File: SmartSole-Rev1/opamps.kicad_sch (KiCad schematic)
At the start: 19 parts, among them U1 MCP6004, U2 MCP6004, U3 AD1583

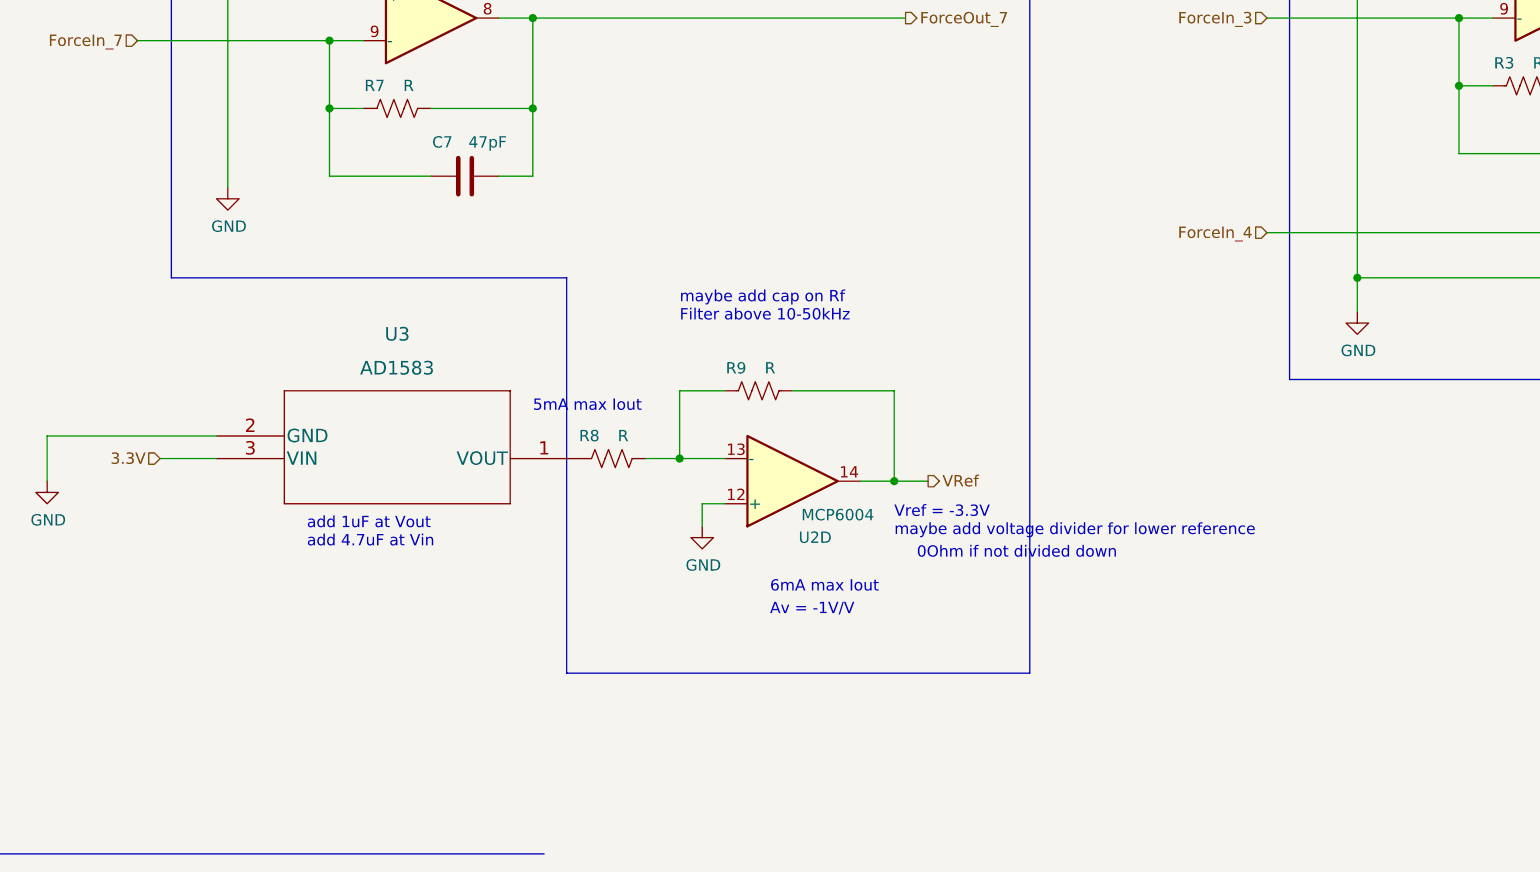
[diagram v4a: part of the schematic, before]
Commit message: Completed updates for schematic and PCB as noted from last review with rachel, DRC only warnings
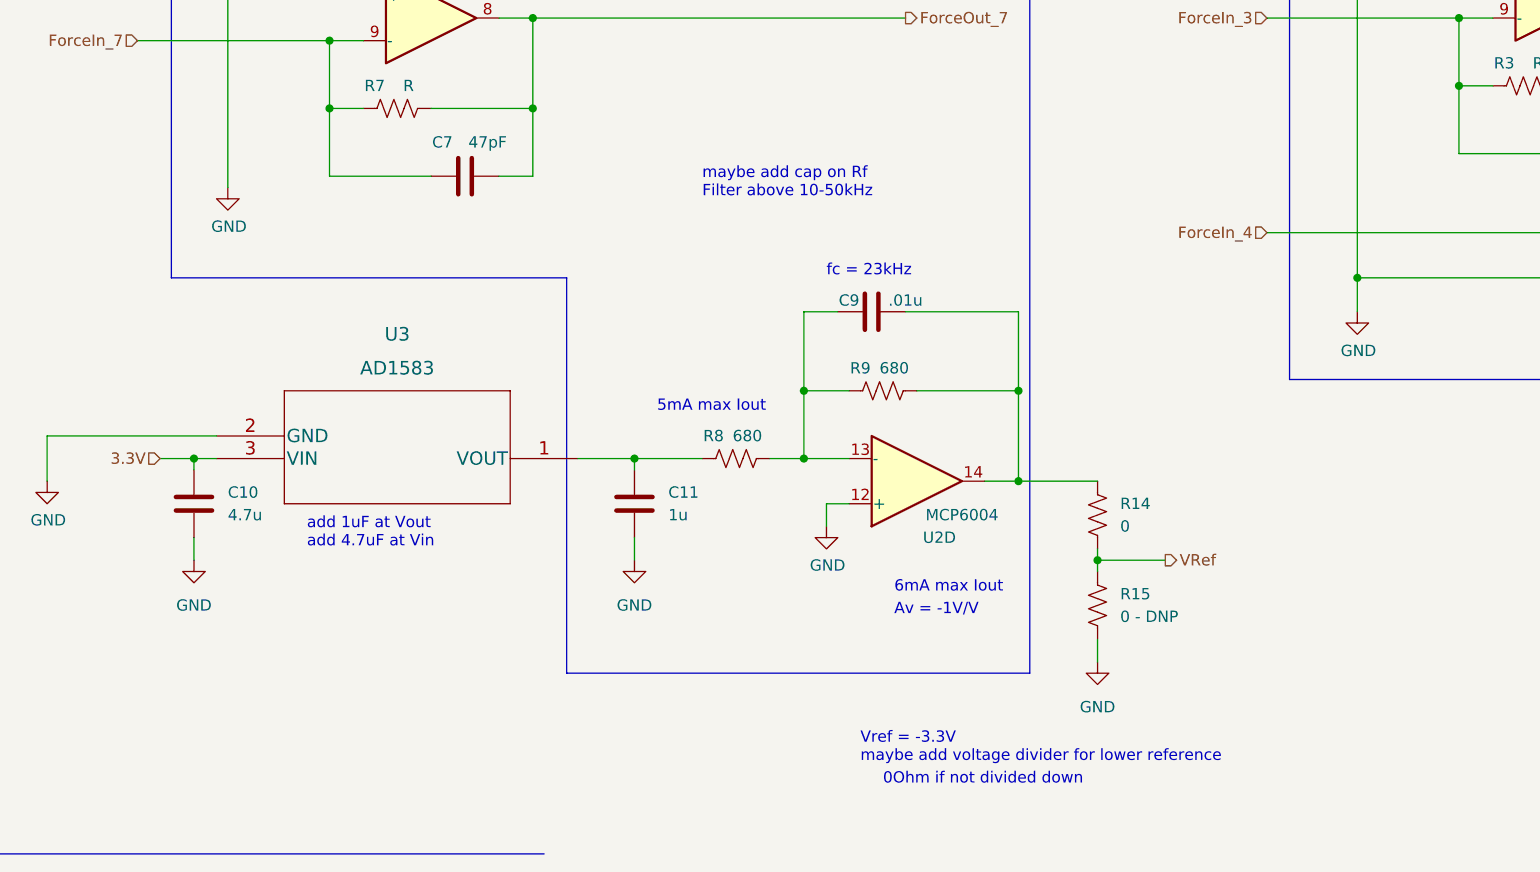
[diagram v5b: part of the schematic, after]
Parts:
- added C10: 4.7u, Capacitor_SMD:C_0603_1608Metric, symbol Device:C
- added C11: 1u, Capacitor_SMD:C_0603_1608Metric, symbol Device:C
- added C9: .01u, Capacitor_SMD:C_0603_1608Metric, symbol Device:C
- added R14: 0, Resistor_SMD:R_0603_1608Metric, symbol Device:R_US
- added R15: 0 - DNP, Resistor_SMD:R_0603_1608Metric, symbol Device:R_US
- R8, R9: value R -> 680
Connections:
- net 3.3V: now also C10.1
- net GND: now also C10.2, C11.2, R15.2
- net VRef: now also R14.1, R15.1; no longer R9.2, U2.14
- net at R8.2, R9.1, U2.13 (-): now also C9.1
- net at R8.1, U3.1 (VOUT): now also C11.1
- new net: C9.2, R14.2, R9.2, U2.14
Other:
- note added: "fc = 23kHz"
- moved on the sheet: R8, R9, U2D

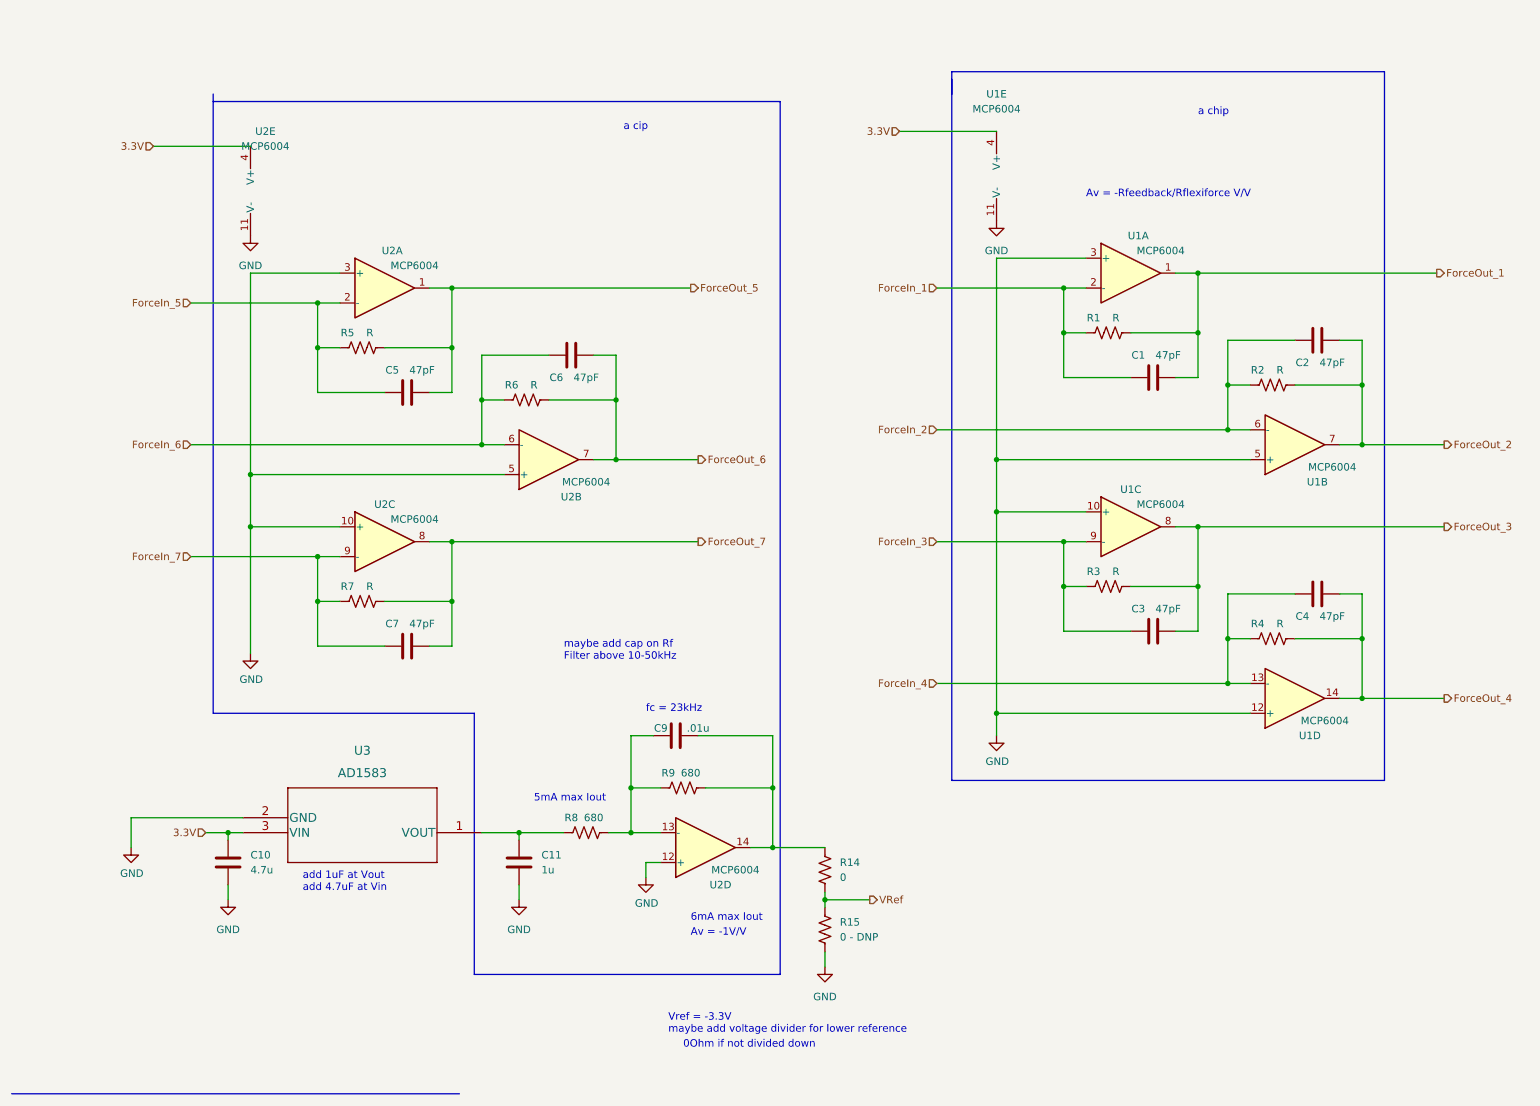
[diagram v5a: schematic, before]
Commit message: changed to non-inverting config
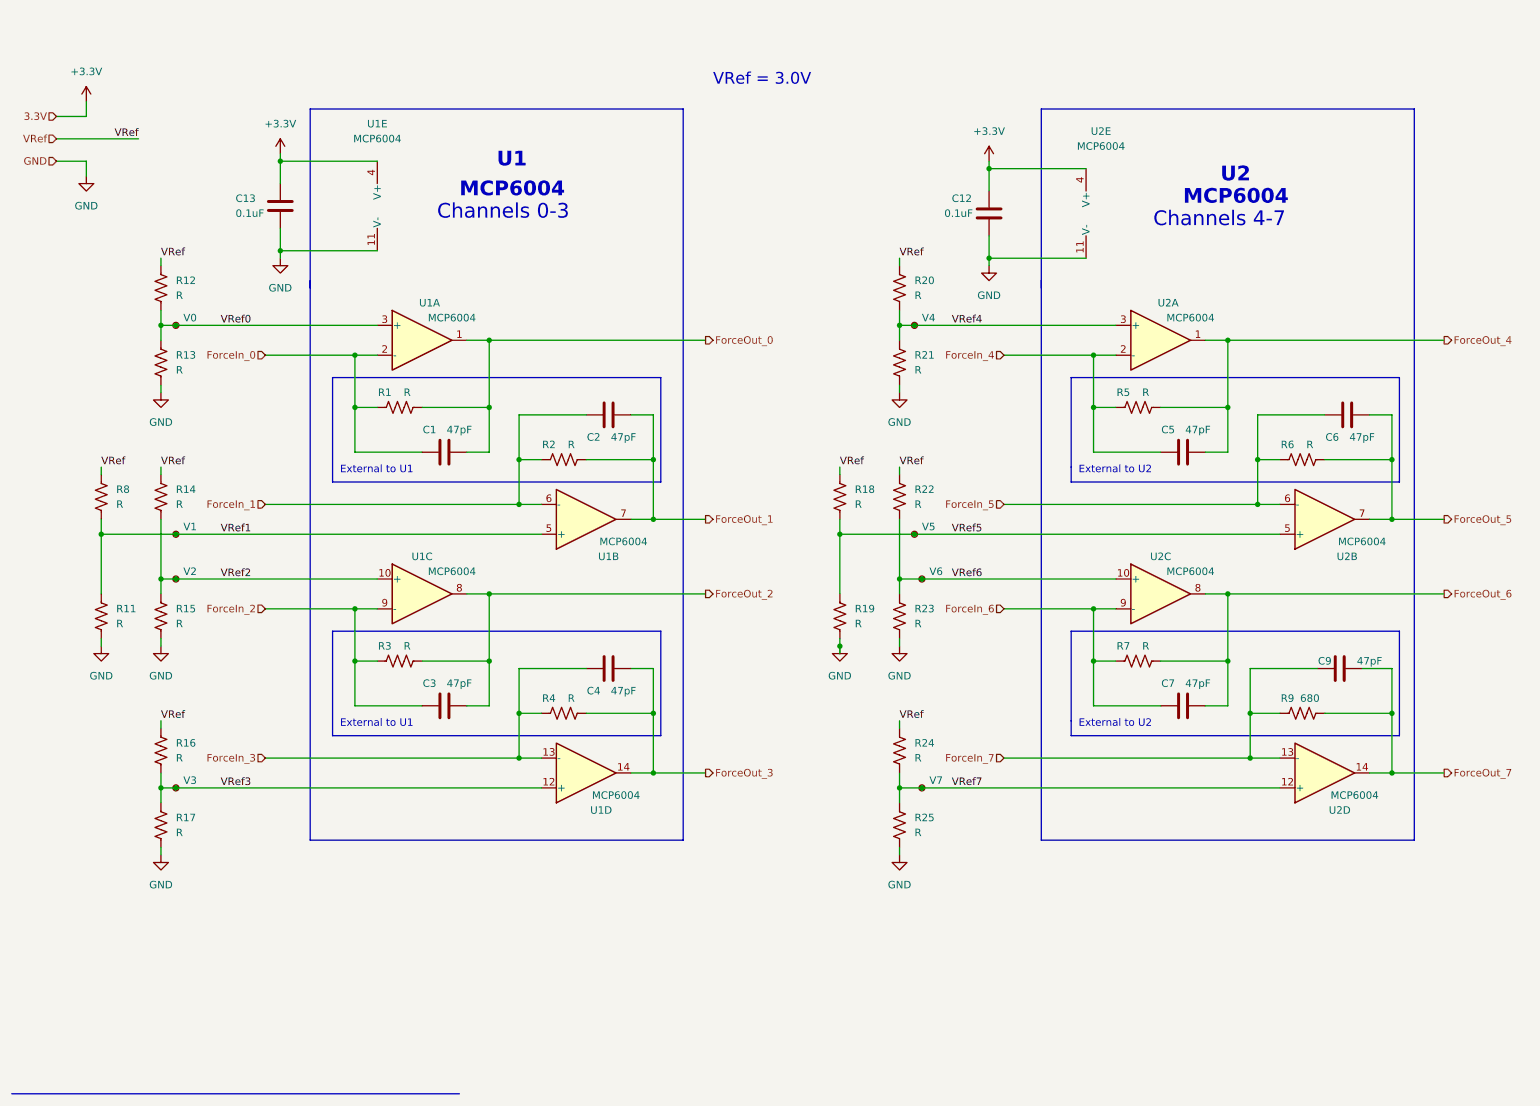
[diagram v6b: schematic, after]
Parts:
- removed C10: 4.7u, Capacitor_SMD:C_0603_1608Metric, symbol Device:C
- removed C11: 1u, Capacitor_SMD:C_0603_1608Metric, symbol Device:C
- removed U3: AD1583, CapstoneLibrary:AD1583ARTZ-Reel7, symbol CapstoneLibrary:AD1583
- added C12, C13: 0.1uF, Capacitor_SMD:C_0603_1608Metric, symbol Device:C
- added R11, R12, R13, R16, R17, R18, R19, R20, R21, R22, R23, R24, R25: R, Resistor_SMD:R_0603_1608Metric, symbol Device:R_US
- added V0, V1, V2, V3, V4, V5, V6, V7: TestPoint_Small, TestPoint:TestPoint_THTPad_1.5x1.5mm_Drill0.7mm, symbol Connector:TestPoint_Small
- C9: value .01u -> 47pF
- R14: value 0 -> R
- R15: value 0 - DNP -> R
- R8: value 680 -> R
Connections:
- net ForceIn_1: now also C2.2, R2.1, U1.6 (-); no longer C1.2, R1.1, U1.2 (-)
- net ForceIn_2: now also C3.2, R3.1, U1.9 (-); no longer C2.2, R2.1, U1.6 (-)
- net ForceIn_3: now also C4.2, R4.1, U1.13 (-); no longer C3.2, R3.1, U1.9 (-)
- net ForceIn_4: now also C5.2, R5.1, U2.2 (-); no longer C4.2, R4.1, U1.13 (-)
- net ForceIn_5: now also C6.2, R6.1, U2.6 (-); no longer C5.2, R5.1, U2.2 (-)
- net ForceIn_6: now also C7.2, R7.1, U2.9 (-); no longer C6.2, R6.1, U2.6 (-)
- net ForceIn_7: now also C9.1, R9.1, U2.13 (-); no longer C7.2, R7.1, U2.9 (-)
- net ForceOut_1: now also C2.1, R2.2, U1.7; no longer C1.1, R1.2, U1.1
- net ForceOut_2: now also C3.1, R3.2, U1.8; no longer C2.1, R2.2, U1.7
- net ForceOut_3: now also C4.1, R4.2, U1.14; no longer C3.1, R3.2, U1.8
- net ForceOut_4: now also C5.1, R5.2, U2.1; no longer C4.1, R4.2, U1.14
- net ForceOut_5: now also C6.1, R6.2, U2.7; no longer C5.1, R5.2, U2.1
- net ForceOut_6: now also C7.1, R7.2, U2.8; no longer C6.1, R6.2, U2.7
- net ForceOut_7: now also C9.2, R9.2, U2.14; no longer C7.1, R7.2, U2.8
- net GND: now also C12.2, C13.2, R11.2, R13.2, R17.2, R19.2, R21.2, R23.2, R25.2; no longer U1.10 (+), U1.12 (+), U1.3 (+), U1.5 (+), U2.10 (+), U2.12 (+), U2.3 (+), U2.5 (+)
- net VRef: now also R8.1, R12.1, R16.1, R18.1, R20.1, R22.1, R24.1; no longer R15.1
- net 3.3V renamed +3V3
- net +3V3: now also C12.1, C13.1
- new net ForceIn_0: C1.2, R1.1, U1.2 (-)
- new net ForceOut_0: C1.1, R1.2, U1.1
- new net VRef0: R12.2, R13.1, U1.3 (+), V0.1
- new net VRef1: R11.1, R8.2, U1.5 (+), V1.1
- new net VRef2: R14.2, R15.1, U1.10 (+), V2.1
- new net VRef3: R16.2, R17.1, U1.12 (+), V3.1
- new net VRef4: R20.2, R21.1, U2.3 (+), V4.1
- new net VRef5: R18.2, R19.1, U2.5 (+), V5.1
- new net VRef6: R22.2, R23.1, U2.10 (+), V6.1
- new net VRef7: R24.2, R25.1, U2.12 (+), V7.1
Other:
- note added: "Channels 0-3"
- note added: "Channels 4-7"
- note added: "External to U1"
- note added: "External to U2"
- note added: "MCP6004"
- note added: "U1"
- note added: "U2"
- note added: "VRef = 3.0V"
- note removed: "0Ohm if not divided down"
- note removed: "5mA max Iout"
- note removed: "6mA max Iout"
- note removed: "Av = -1V/V"
- note removed: "Av = -Rfeedback/Rflexiforce V/V"
- note removed: "Vref = -3.3V maybe add voltage divider for lower reference"
- note removed: "a chip"
- note removed: "a cip"
- note removed: "add 1uF at Vout add 4.7uF at Vin"
- note removed: "fc = 23kHz"
- note removed: "maybe add cap on Rf Filter above 10-50kHz"
- moved on the sheet: C1, C2, C3, C4, C5, C6, C7, C9, R1, R2, R3, R4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

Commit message: changed to single coltage reference per opamp IC
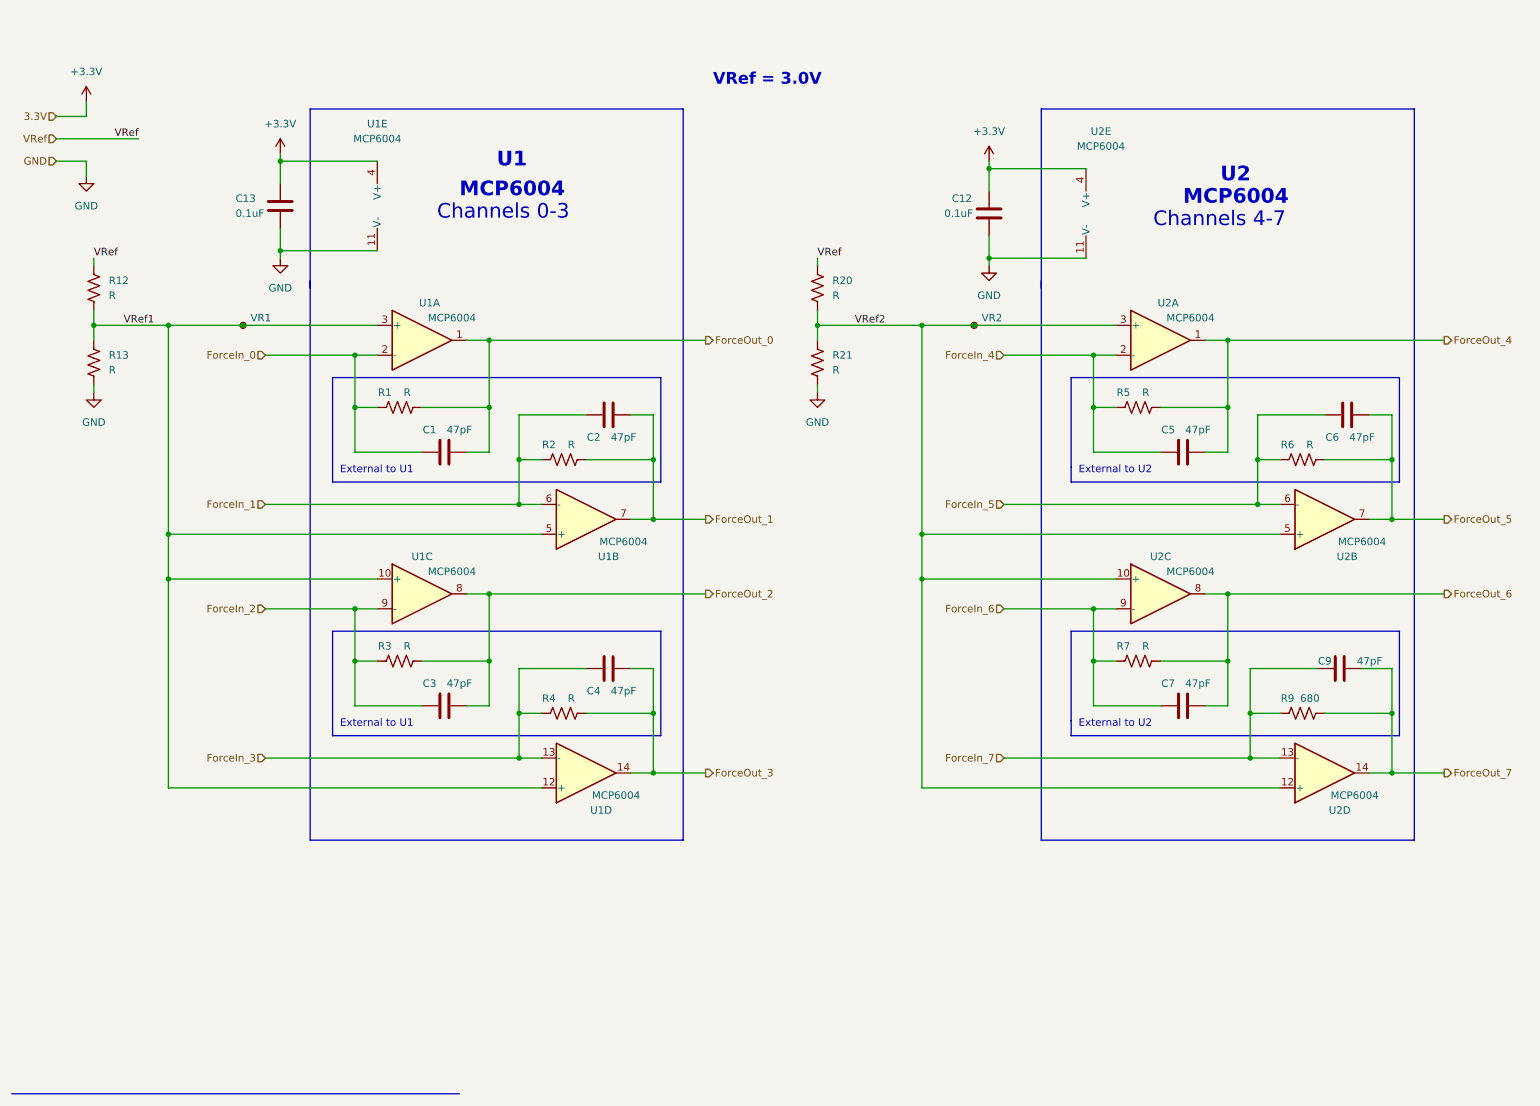
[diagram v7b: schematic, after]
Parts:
- removed R11, R14, R15, R16, R17, R18, R19, R22, R23, R24, R25, R8: R, Resistor_SMD:R_0603_1608Metric, symbol Device:R_US
- removed V1, V2, V3, V5, V6, V7: TestPoint_Small, TestPoint:TestPoint_THTPad_1.5x1.5mm_Drill0.7mm, symbol Connector:TestPoint_Small
- renumbered V0 to VR1, V4 to VR2
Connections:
- net VRef0 is gone; now on net VRef1: R12.2, R13.1, U1.3 (+), VR1.1
- net VRef3 is gone; now on net VRef1: U1.12 (+)
- net VRef4 is gone; now on net VRef2: R20.2, R21.1, U2.3 (+), VR2.1
- net VRef5 is gone; now on net VRef2: U2.5 (+)
- net VRef6 is gone; now on net VRef2: U2.10 (+)
- net VRef7 is gone; now on net VRef2: U2.12 (+)
- net VRef1: now also U1.10 (+)
- net VRef2: no longer U1.10 (+)
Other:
- moved on the sheet: R12, R13, R20, R21, VR1, VR2

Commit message: final layout
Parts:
- R9: value 680 -> R
- VR1, VR2: footprint TestPoint:TestPoint_THTPad_1.5x1.5mm_Drill0.7mm -> SmartSoleFPs:TestPoint_Loop_D0.8mm_Dril0.4mm
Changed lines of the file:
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@@
       (effects (font (size 1.27 1.27)) (justify left) hide)
     )
-    (property "Footprint" "TestPoint:TestPoint_THTPad_1.5x1.5mm_Drill0.7mm" (id 2) (at 63.5 68.58 0)
+    (property "Footprint" "SmartSoleFPs:TestPoint_Loop_D0.8mm_Dril0.4mm" (id 2) (at 63.5 68.58 0)
       (effects (font (size 1.27 1.27)) hide)
     )
@@
       (effects (font (size 1.27 1.27)) (justify left) hide)
     )
-    (property "Footprint" "TestPoint:TestPoint_THTPad_1.5x1.5mm_Drill0.7mm" (id 2) (at 187.96 68.58 0)
+    (property "Footprint" "SmartSoleFPs:TestPoint_Loop_D0.8mm_Dril0.4mm" (id 2) (at 187.96 68.58 0)
       (effects (font (size 1.27 1.27)) hide)
     )
@@
     (in_bom yes) (on_board yes)
     (property "Reference" "R9" (id 0) (at 236.22 132.08 90))
-    (property "Value" "680" (id 1) (at 240.03 132.08 90))
+    (property "Value" "R" (id 1) (at 240.03 132.08 90))
     (property "Footprint" "Resistor_SMD:R_0603_1608Metric" (id 2) (at 239.014 133.604 90)
       (effects (font (size 1.27 1.27)) hide)
